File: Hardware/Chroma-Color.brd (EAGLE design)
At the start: 106.4 x 50.5 mm, 92 parts, among them J1 15-91-1102, J2 87832-6422, J3 1775470-6, J4 D2514-6V0C-AR-WD, J7 26-64-4040, U1 EP4CE6E22C8N, U2 ADP3338AKCZ-3.3-RL, U3 ADP3338AKCZ-2.5-RL, U4 NCV565ST12T3G, U5 M25P40-VMN6TPBCT, X1 ASDMB-50.000MHZ-LC-T

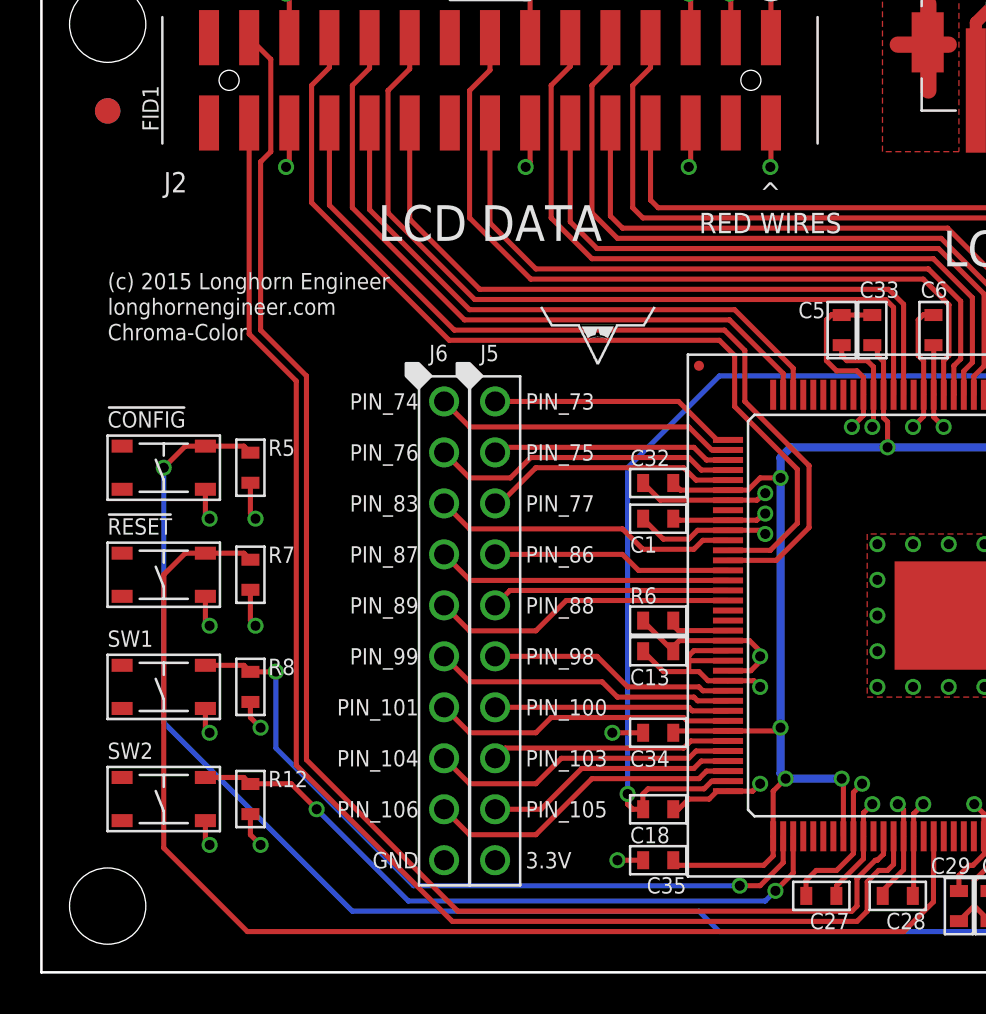
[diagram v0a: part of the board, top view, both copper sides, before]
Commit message: Added SW3. Need to add a buffer/level shifter.
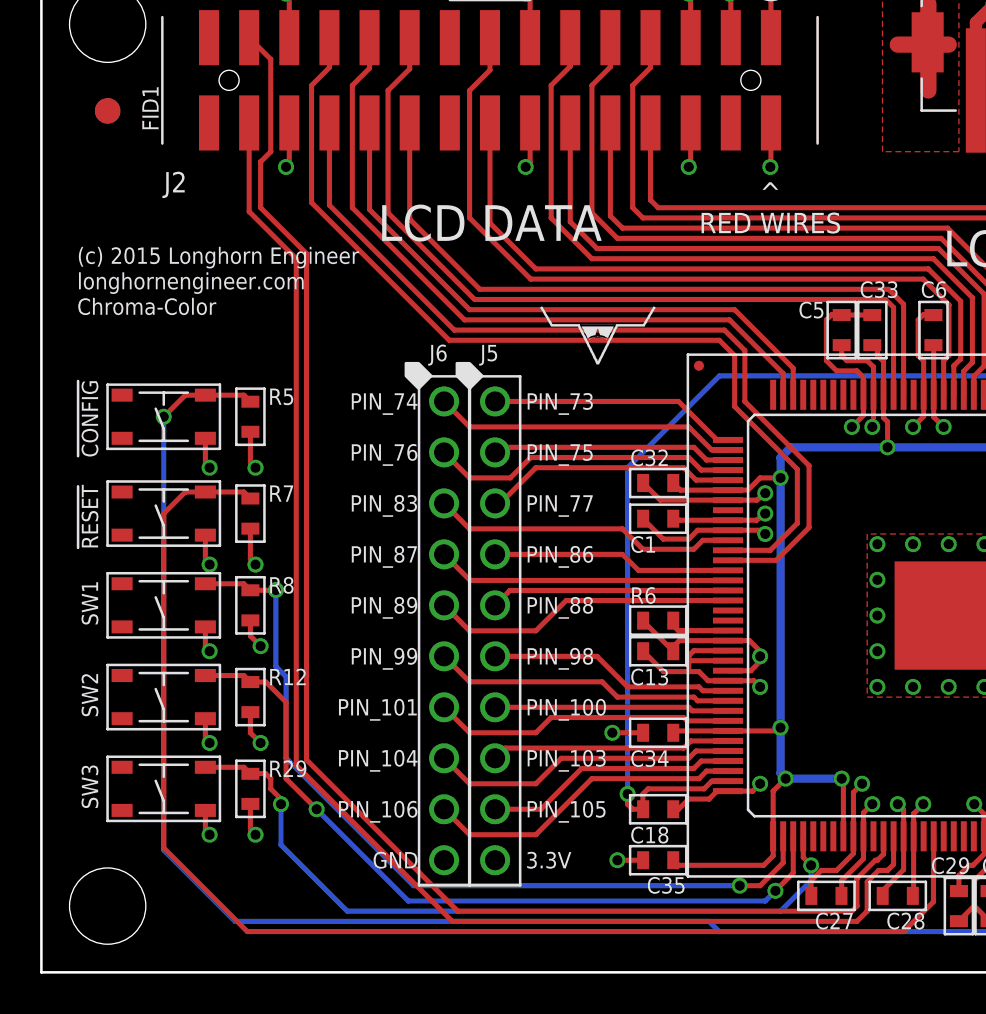
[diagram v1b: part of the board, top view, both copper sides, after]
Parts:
- added R29: 10K, MF_Passives:R0603
- added SW3: (no value), MF_Switches:TACT4.2MM
- moved R12 5.08 mm to (10.4, 13.7)
- moved SW2 5.08 mm to (6.10, 13.7)
- moved R8 4.06 mm to (10.4, 18.3)
- moved SW1 4.06 mm to (6.10, 18.3)
- moved !RESET 3.05 mm to (6.10, 22.9)
- moved R7 3.05 mm to (10.4, 22.9)
- moved !CONFIG 2.54 mm to (6.10, 27.7)
- moved R5 2.54 mm to (10.4, 27.7)
- moved U$1 1.98 mm to (1.78, 30.2)
- moved C27 0.25 mm to (39.1, 3.81)
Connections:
- net 3.3V: now also R29.P$1
- net GND: now also SW3.P$4
- net PIN_112: now also R29.P$2, SW3.P$2
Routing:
- net PIN_112: track 0.00 -> 37.8 mm, vias 0 -> 2
- net !CONFIG: track 95.6 -> 101.8 mm
- net PIN_111: track 34.3 -> 38.6 mm
- net PIN_110: track 37.4 -> 41.4 mm
- net RESET: track 62.5 -> 65.5 mm
- net GND: track 268.0 -> 269.7 mm, vias 78 -> 79
- net 3.3V: track 119.7 -> 121.4 mm, vias 50 -> 51

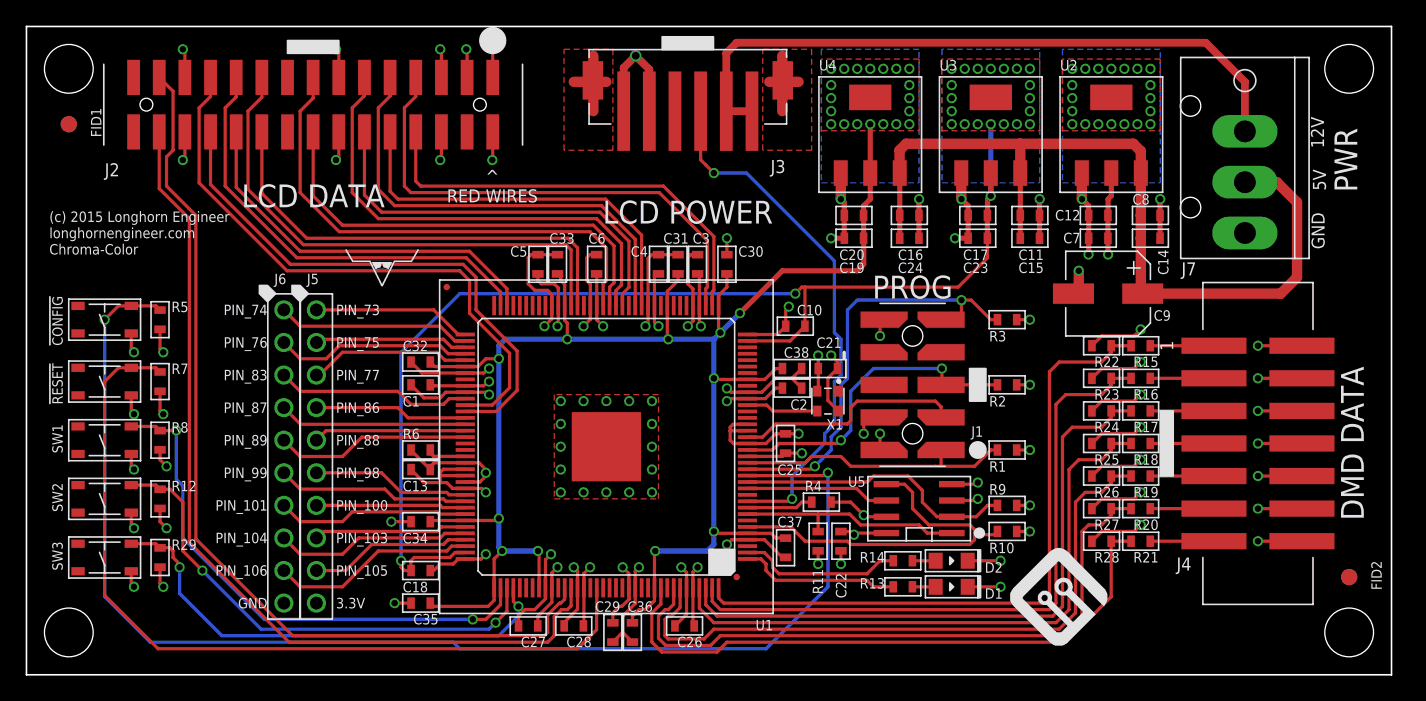
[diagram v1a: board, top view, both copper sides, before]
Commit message: Working on adding level shifter and LVDS 3 R
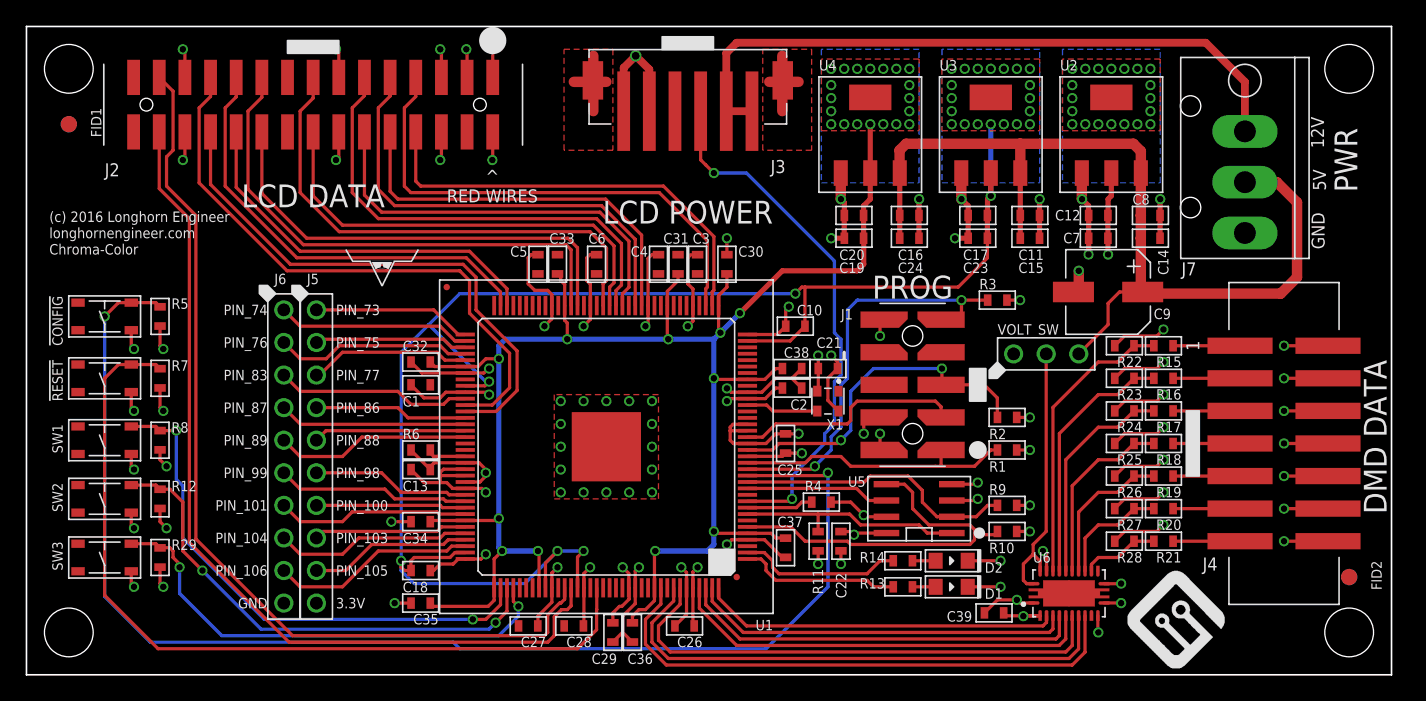
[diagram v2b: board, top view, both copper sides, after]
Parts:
- added C39: 0.1uF, MF_Passives:C0603
- added U6: SN74LVC8T245RHLR, PP_DigitalIC:SN74LVC8T245_VQFN-24
- added VOLT_SW: (no value), MF_Connectors:PTH_2.54MM_01X03
- moved U$2 9.32 mm to (85.9, 0.51)
- moved R2 2.54 mm to (76.5, 20.1)
- moved J4 2.03 mm to (98.0, 18.0)
- moved R15 1.78 mm to (88.6, 25.7)
- moved R16 1.78 mm to (88.6, 23.1)
- moved R17 1.78 mm to (88.6, 20.6)
- moved R18 1.78 mm to (88.6, 18.0)
- moved R19 1.78 mm to (88.6, 15.5)
- moved R20 1.78 mm to (88.6, 13.0)
- moved R21 1.78 mm to (88.6, 10.4)
- moved R22 1.78 mm to (85.6, 25.7)
- moved R23 1.78 mm to (85.6, 23.1)
- moved R24 1.78 mm to (85.6, 20.6)
- moved R25 1.78 mm to (85.6, 18.0)
- moved R26 1.78 mm to (85.6, 15.5)
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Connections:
- new net CLOCK_LS: U1.144, U6.3
- new net DATA_LS: U1.143, U6.4
- new net ENABLE_LS: U1.135, U6.9
- new net LATCH_LS: U1.142, U6.5
- new net REG0_LS: U1.137, U6.8
- new net REG1_LS: U1.138, U6.7
- new net REG2_LS: U1.141, U6.6
- new net VCCB: U6.23, U6.24, VOLT_SW.P$2
- net 2.5V: now also C1.P$1, C27.P$1, C28.P$1, C3.P$1, C4.P$1, C5.P$1, C6.P$1, U1.117, U1.122, U1.40, U1.47, U1.56, U1.62, U1.81
- net 3.3V: now also C39.P$1, U6.1, VOLT_SW.P$1; no longer C1.P$1, C27.P$1, C28.P$1, C3.P$1, C4.P$1, C5.P$1, C6.P$1, U1.117, U1.122, U1.40, U1.47, U1.56, U1.62, U1.81
- net 5V: now also VOLT_SW.P$3
- net CLOCK: now also U6.21; no longer U1.144
- net DATA: now also U6.20; no longer U1.143
- net ENABLE: now also U6.15; no longer U1.135
- net GND: now also C39.P$2, U6.11, U6.12, U6.13, U6.2, U6.22
- net LATCH: now also U6.19; no longer U1.142
- net REG0: now also U6.16; no longer U1.137
- net REG1: now also U6.17; no longer U1.138
- net REG2: now also U6.18; no longer U1.141
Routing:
- net ENABLE_LS: track 0.00 -> 43.1 mm
- net ENABLE: track 48.3 -> 6.12 mm
- net REG0_LS: track 0.00 -> 41.9 mm
- net REG0: track 50.2 -> 8.87 mm
- net REG1_LS: track 0.00 -> 39.9 mm
- net REG1: track 51.4 -> 11.6 mm
- net REG2: track 48.2 -> 14.4 mm
- net REG2_LS: track 0.00 -> 33.4 mm
- net LATCH: track 49.5 -> 17.1 mm
- net 3.3V: track 121.4 -> 89.7 mm, vias 51 -> 45
- net LATCH_LS: track 0.00 -> 31.6 mm
- net 2.5V: track 92.0 -> 123.3 mm, vias 23 -> 26
- net DATA: track 50.8 -> 19.9 mm
- net DATA_LS: track 0.00 -> 29.8 mm
- net CLOCK: track 52.1 -> 22.6 mm
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
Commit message: REV 2 done.
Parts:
- removed FID3: FIDUCIAL_0.5MM, MF_Aesthetics:FIDUCIAL_0.5MM
- added R30, R31, R33, R34, R36, R37, R39, R40, R42, R43, R45, R46, R48, R49, R51, R52: 120, MF_Passives:R0402
- added R32, R35, R38, R41, R44, R47, R50, R53: 170, MF_Passives:R0402
- moved U$2 77.0 mm to (8.89, 0.51)
- moved U$1 67.0 mm to (59.9, -3.05)
- moved U$3 21.6 mm to (8.13, 30.5)
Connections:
- new net EVEN0+_RN: J2.P$20, R42.P$2, R44.P$2
- new net EVEN0-_RN: J2.P$19, R43.P$2, R44.P$1
- new net EVEN1+_RN: J2.P$22, R45.P$2, R47.P$2
- new net EVEN1-_RN: J2.P$21, R46.P$2, R47.P$1
- new net EVEN2+_RN: J2.P$24, R48.P$2, R50.P$2
- new net EVEN2-_RN: J2.P$23, R49.P$2, R50.P$1
- new net EVENC+_RN: J2.P$28, R51.P$2, R53.P$2
- new net EVENC-_RN: J2.P$27, R52.P$2, R53.P$1
- new net ODD0+_RN: J2.P$8, R31.P$2, R32.P$2
- new net ODD0-_RN: J2.P$7, R30.P$2, R32.P$1
- new net ODD1+_RN: J2.P$10, R33.P$2, R35.P$2
- new net ODD1-_RN: J2.P$9, R34.P$2, R35.P$1
- new net ODD2+_RN: J2.P$12, R36.P$2, R38.P$2
- new net ODD2-_RN: J2.P$11, R37.P$2, R38.P$1
- new net ODDC+_RN: J2.P$16, R39.P$2, R41.P$2
- new net ODDC-_RN: J2.P$15, R40.P$2, R41.P$1
- net 2.5V: now also R12.P$1, R29.P$1, R7.P$1, R8.P$1
- net 3.3V: no longer R12.P$1, R29.P$1, R7.P$1, R8.P$1
- net EVEN0+: now also R42.P$1; no longer J2.P$20
- net EVEN0-: now also R43.P$1; no longer J2.P$19
- net EVEN1+: now also R45.P$1; no longer J2.P$22
- net EVEN1-: now also R46.P$1; no longer J2.P$21
- net EVEN2+: now also R48.P$1; no longer J2.P$24
- net EVEN2-: now also R49.P$1; no longer J2.P$23
- net EVENC+: now also R51.P$1; no longer J2.P$28
- net EVENC-: now also R52.P$1; no longer J2.P$27
- net ODD0+: now also R31.P$1; no longer J2.P$8
- net ODD0-: now also R30.P$1; no longer J2.P$7
- net ODD1+: now also R33.P$1; no longer J2.P$10
- net ODD1-: now also R34.P$1; no longer J2.P$9
- net ODD2+: now also R36.P$1; no longer J2.P$12
- net ODD2-: now also R37.P$1; no longer J2.P$11
- net ODDC+: now also R39.P$1; no longer J2.P$16
- net ODDC-: now also R40.P$1; no longer J2.P$15
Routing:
- net 2.5V: track 123.3 -> 201.0 mm, vias 26 -> 34
- net ODD0-: track 39.3 -> 28.0 mm
- net ODD0-_RN: track 0.00 -> 10.6 mm
- net EVENC-: track 72.3 -> 62.3 mm
- net ODDC-_RN: track 0.00 -> 9.35 mm
- net EVEN0-_RN: track 0.00 -> 8.89 mm
- net ODD2-_RN: track 0.00 -> 8.63 mm
- net 3.3V: track 89.7 -> 81.2 mm, vias 45 -> 40
- net EVENC-_RN: track 0.00 -> 8.53 mm
- net EVEN1-_RN: track 0.00 -> 8.49 mm
- net ODD1-_RN: track 0.00 -> 8.45 mm
- net EVEN2-_RN: track 0.00 -> 8.40 mm
- net EVEN0-: track 40.7 -> 32.3 mm
- net ODD1-: track 35.9 -> 27.9 mm
- net EVEN1-: track 34.8 -> 26.8 mm
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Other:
- board size 106.4 x 50.5 mm -> 106.7 x 50.5 mm
- board text added: "RED WIRES"
- board text removed: "^ RED WIRES"

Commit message: Added manufacturing gerbers.
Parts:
- VOLT_SW: value (none) -> 4-103321-5
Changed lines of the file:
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@@
 <?xml version="1.0" encoding="utf-8"?>
 <!DOCTYPE eagle SYSTEM "eagle.dtd">
-<eagle version="6.6.0">
+<eagle version="6.5.0">
 <drawing>
 <settings>
@@
 <attribute name="NAME" x="71.752" y="4.148" size="0.8128" layer="25" font="vector" ratio="16"/>
 </element>
-<element name="VOLT_SW" library="MF_Connectors" package="PTH_2.54MM_01X03" value="" x="79.502" y="25.019">
+<element name="VOLT_SW" library="MF_Connectors" package="PTH_2.54MM_01X03" value="4-103321-5" x="79.502" y="25.019">
 <attribute name="LABEL02" value="5V" x="79.502" y="25.019" size="1.778" layer="27" display="off"/>
 <attribute name="LABEL00" value="3.3V" x="79.502" y="25.019" size="1.778" layer="27" display="off"/>
